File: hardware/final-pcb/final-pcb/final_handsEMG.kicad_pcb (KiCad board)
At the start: 2 copper layers, 47 parts, among them J1 Conn_02x13_Odd_Even, U1 ADS1299CPAG

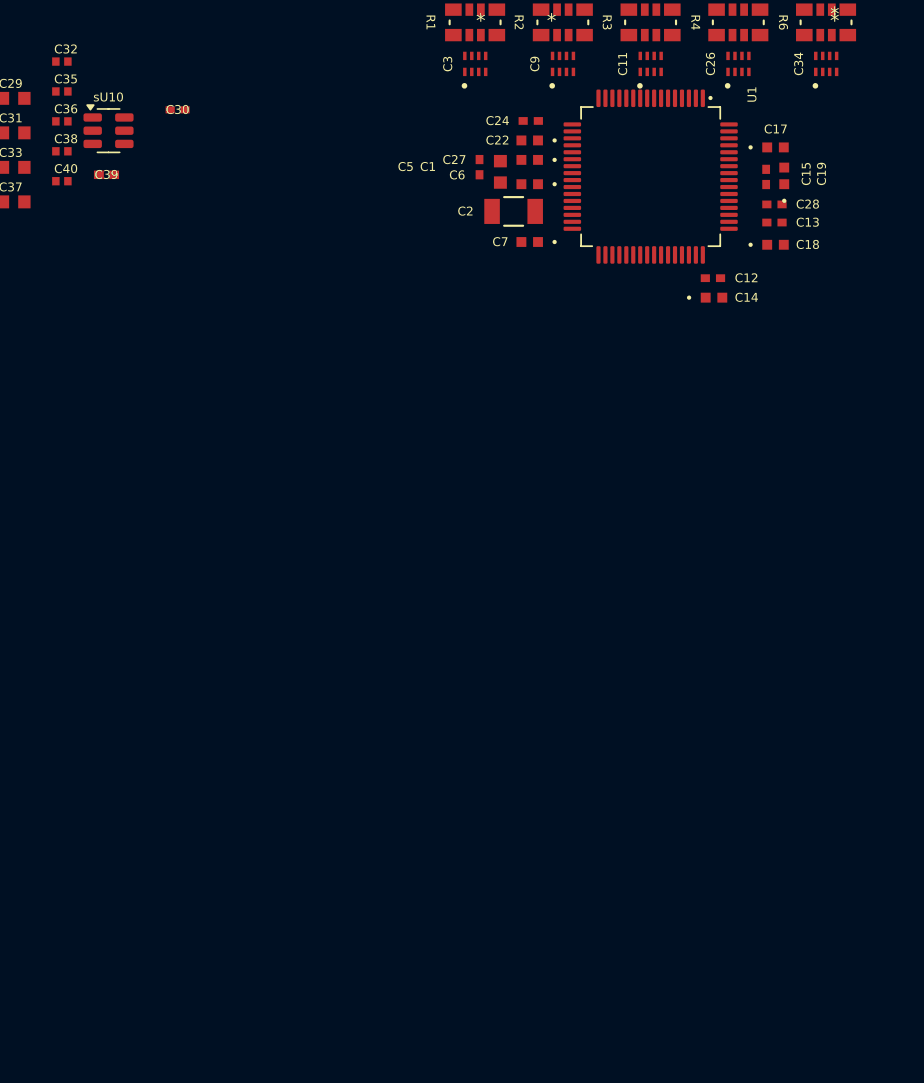
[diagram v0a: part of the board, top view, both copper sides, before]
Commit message: added stm32 decoupling circuitry and usb (3.24.25)
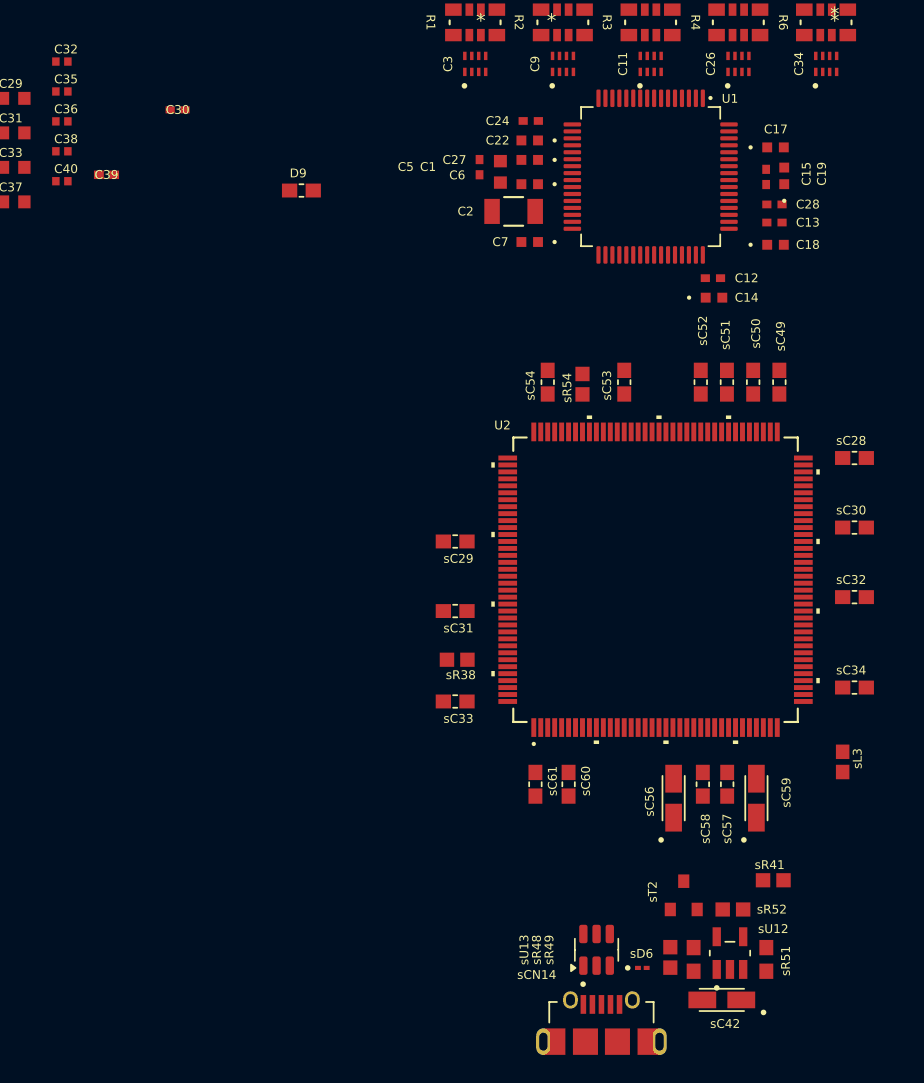
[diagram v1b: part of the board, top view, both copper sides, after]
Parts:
- added D9: D_Small, CC0603KRX7R7BB104:CAPC1608X90, F.Cu at (80.4, 62.0)
- added U2: STM32L496ZGT6, STM32L496ZGT6:LQFP144-20x20mm_STM, F.Cu at (105.8, 90.0)
- added sC28: 100nF, CC0603KRX7R7BB104:CAPC1608X90, F.Cu at (120.2, 81.2)
- added sC29: 100nF, CC0603KRX7R7BB104:CAPC1608X90, F.Cu at (91.5, 87.2)
- added sC30: 100nF, CC0603KRX7R7BB104:CAPC1608X90, F.Cu at (120.2, 86.2)
- added sC31: 100nF, CC0603KRX7R7BB104:CAPC1608X90, F.Cu at (91.5, 92.2)
- added sC32: 100nF, CC0603KRX7R7BB104:CAPC1608X90, F.Cu at (120.2, 91.2)
- added sC33: 100nF, CC0603KRX7R7BB104:CAPC1608X90, F.Cu at (91.5, 98.7)
- added sC34: 100nF, CC0603KRX7R7BB104:CAPC1608X90, F.Cu at (120.2, 97.7)
- added sC42: 4.7uF, TAJA475K016R:CAPMP3216X166, F.Cu at (110.6, 120.2)
- added sC49: 100nF, CC0603KRX7R7BB104:CAPC1608X90, F.Cu at (114.8, 75.8)
- added sC50: 100nF, CC0603KRX7R7BB104:CAPC1608X90, F.Cu at (112.9, 75.8)
- added sC51: 100nF, CC0603KRX7R7BB104:CAPC1608X90, F.Cu at (111.0, 75.8)
- added sC52: 4.7uF_X54_0603, CC0603KRX5R7BB475:CAPC1608X90, F.Cu at (109.1, 75.8)
- added sC53: 100nF, CC0603KRX7R7BB104:CAPC1608X90, F.Cu at (103.6, 75.8)
- added sC54: 4.7uF_X54_0603, CC0603KRX5R7BB475:CAPC1608X90, F.Cu at (98.1, 75.8)
- added sC56: 1uF, TAJA105K016R:CAPMP3216X166, F.Cu at (107.2, 105.7)
- added sC57: 100nF, CC0603KRX7R7BB104:CAPC1608X90, F.Cu at (111.0, 104.7)
- added sC58: 100nF, CC0603KRX7R7BB104:CAPC1608X90, F.Cu at (109.2, 104.7)
- added sC59: 1uF, TAJA105K016R:CAPMP3216X166, F.Cu at (113.1, 105.7)
- added sC60: 1uF_X5R_0603, CC0603KRX5R7BB105:CAPC1608X90, F.Cu at (99.6, 104.7)
- added sC61: 100nF, CC0603KRX7R7BB104:CAPC1608X90, F.Cu at (97.2, 104.7)
- added sCN14: USB_B_Micro, 47589-1001:MOLEX_47589-1001, F.Cu at (102.0, 123.5)
- added sD6: ESDALC6V1_1U2, ESDALC6V1-1U2:DIODE_ESDALC6V1-1U2, F.Cu at (104.9, 117.9)
- added sL3: FerriteBead_Small, FCM1608KF-601T05:FB0603, F.Cu at (119.3, 103.1)
- added sR38: 10K, RC0603FR-0710KL:RESC1607X60N, F.Cu at (91.6, 95.7)
- added sR41: 330, RC0603FR-07330RL:RESC1607X60N, F.Cu at (114.3, 111.6)
- added sR48: 22K, RC0603FR-0722KL:RESC1607X60N, F.Cu at (106.9, 117.1)
- added sR49: 47K, RC0603FR-0747KL:RESC1608X55, F.Cu at (108.6, 117.3)
- added sR51: 47K, RC0603FR-0747KL:RESC1608X55, F.Cu at (113.8, 117.3)
- added sR52: 10K, RC0603FR-0710KL:RESC1607X60N, F.Cu at (111.4, 113.7)
- added sR54: 10K, RC0603FR-0710KL:RESC1607X60N, F.Cu at (100.6, 75.9)
- added sT2: 9013, MMBT9013:SOT-23, F.Cu at (107.9, 112.7)
- added sU12: STMPS2151STR, STMPS2151STR:SOT95P280X145-5N, F.Cu at (111.2, 116.8)
- moved sU13 68.5 mm to (101.6, 116.6), turned to 90 degrees
- renumbered sU10 to sU13
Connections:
- sU13 pad 1: PA12 -> PA11
- sU13 pad 3: PA11 -> PA12
- sU13 pad 4: PA11 -> PA12
- sU13 pad 6: PA12 -> PA11

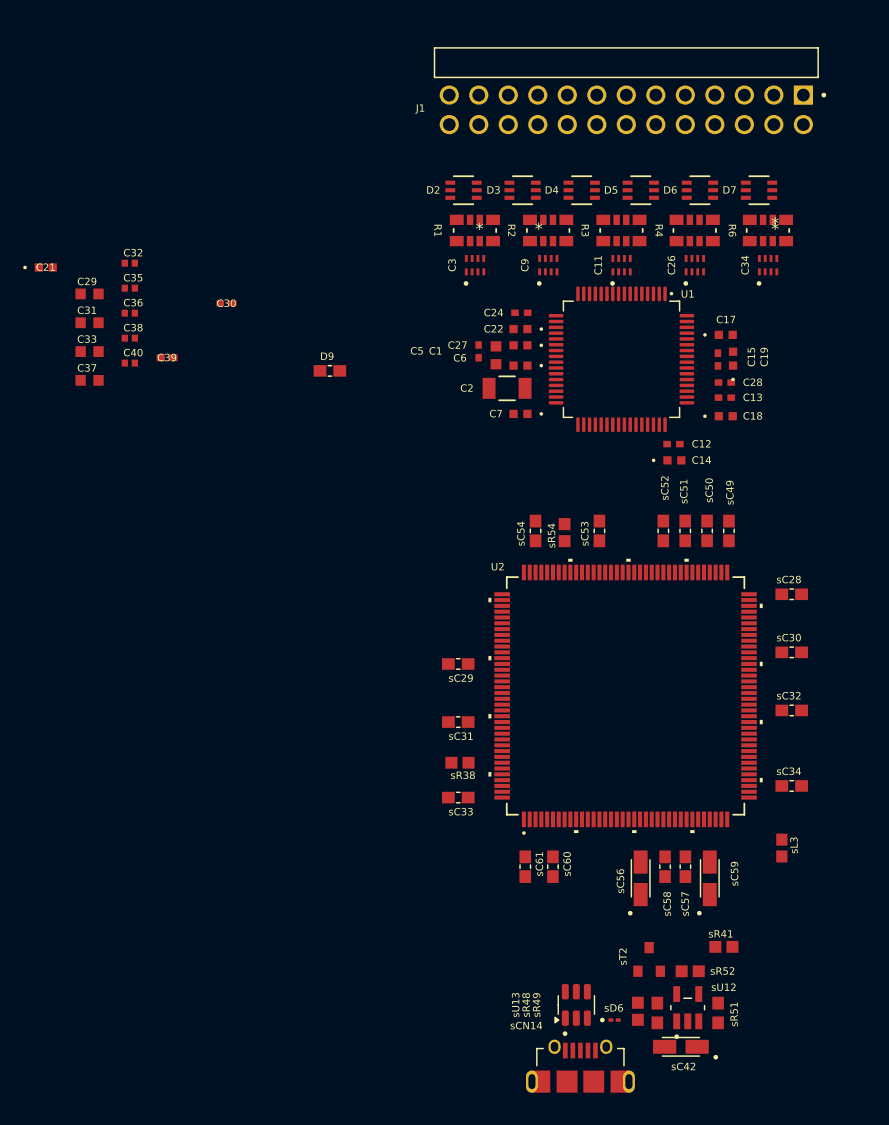
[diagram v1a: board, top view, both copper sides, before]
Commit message: basic routing (3.30.25)
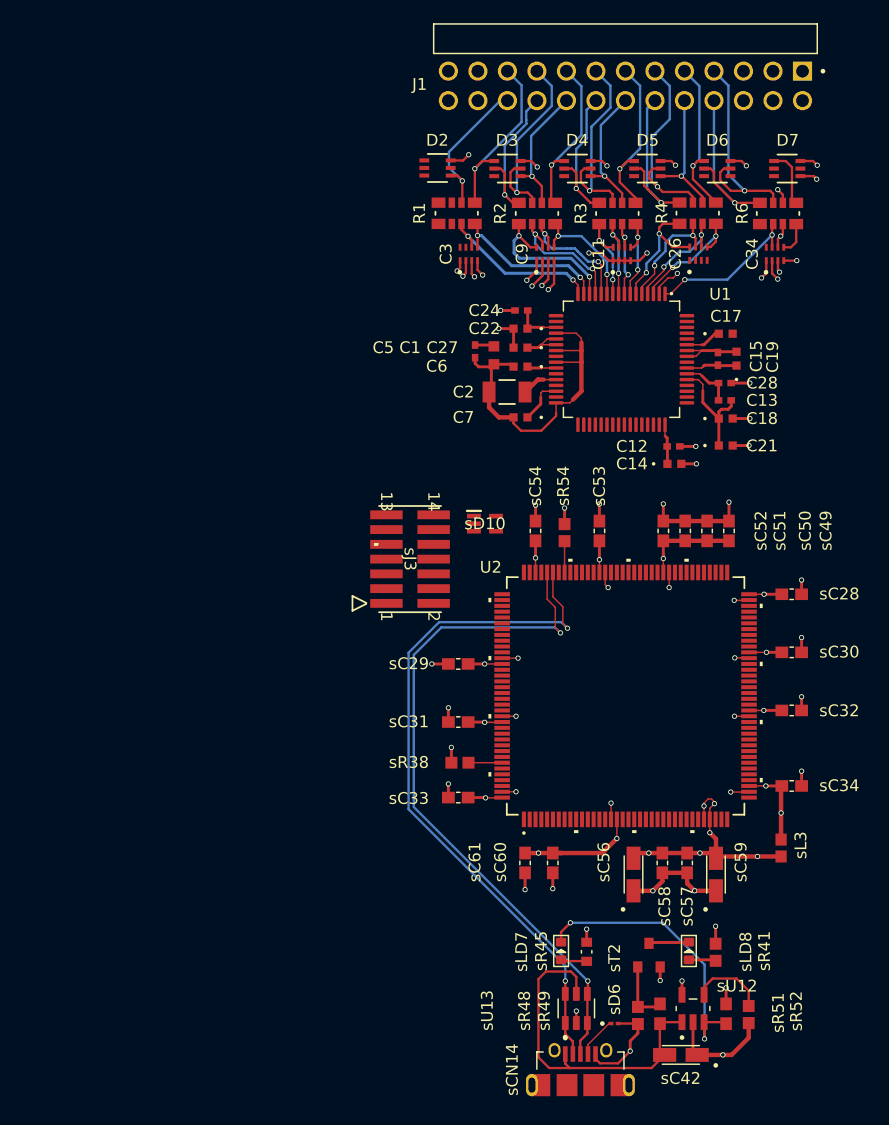
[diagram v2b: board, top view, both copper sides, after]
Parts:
- removed C29, C31, C33, C37: 10uF, GRM188C80G106KE47D:CAPC1608X90N
- removed C30: 0.01uF, CC0402KRX7R7BB103:CC0402N_YAG
- removed C32, C35, C36, C38, C40: 2.2uF, GRM155C80J225ME95D:CAPC1005X55N
- removed C39: 2.2uF, GRM155R61C225KE44D:CAP_GRM155R61C225KE44D_MUR
- removed D9: D_Small, CC0603KRX7R7BB104:CAPC1608X90
- added sD10: ESDALC6V1W5, ESDALC6V1W5:SOT65P210X110-5N, F.Cu at (93.8, 75.2)
- added sJ3: FTSH-107-01-L-DV-K, FTSH_107_01_L_DV_K:CON14_2X7_DUK_FTSH_SAI, F.Cu at (87.3, 78.2)
- added sLD7: Red, LED-SMD-RED-DIFFUSED_0603_:LED-0603, F.Cu at (100.3, 111.9)
- added sLD8: Green, SMD-LED-CLEAR-GREEN_0603_:LED-0603, F.Cu at (111.3, 111.9)
- added sR45: 620, RC0603FR-07620RL:RESC1608X55N, F.Cu at (102.5, 112.0)
- sU13: footprint Package_TO_SOT_SMD:SOT-23-6 -> USBLC6-2SC6:SOT95P280X145-6N
- moved C21 60.5 mm to (114.5, 68.4)
- moved sR52 6.26 mm to (116.5, 117.4), turned to -90 degrees
- moved D7 3.06 mm to (119.8, 44.6)
- moved D2 2.95 mm to (89.7, 44.5)
- moved D6 2.39 mm to (113.7, 44.6)
- moved D3 2.28 mm to (95.7, 44.6)
- moved R1 2.16 mm to (91.3, 48.4)
- moved J1 2.06 mm to (105.8, 33.4)
- moved D5 1.95 mm to (107.7, 44.6)
- moved D4 1.90 mm to (101.7, 44.6)
- moved R2 1.75 mm to (98.2, 48.5)
- moved R6 1.70 mm to (119.0, 48.5)
- moved R4 1.51 mm to (112.1, 48.4)
- moved R3 1.51 mm to (105.1, 48.5)
- moved C34 1.13 mm to (118.7, 51.9)
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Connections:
- net PA11 renamed USB_DN
- net PA12 renamed USB_DP
- U2 pad 25: /NRST -> NRST
- sC42 pad +: (no net) -> USB_VBUS
- sC42 pad -: (no net) -> GND
- sC56 pad -: (no net) -> GNDA
- sC59 pad +: (no net) -> AVDD
- sC59 pad -: (no net) -> GNDA
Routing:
- net GNDA: track 0.00 -> 61.7 mm, vias 0 -> 32
- net USB_DN: track 0.00 -> 60.7 mm, vias 0 -> 2
- net USB_DP: track 0.00 -> 60.3 mm, vias 0 -> 2
- net DVDD: track 0.00 -> 58.4 mm, vias 0 -> 17
- net GND: track 0.00 -> 57.7 mm, vias 0 -> 28
- net AVSS: track 0.00 -> 46.1 mm
- net AVDD: track 0.00 -> 36.8 mm, vias 0 -> 6
- net USB_VBUS: track 0.00 -> 31.2 mm, vias 0 -> 1
- net Net-(sLD7-K): track 0.00 -> 24.8 mm, vias 0 -> 2
- net 8N: track 0.00 -> 18.9 mm, vias 0 -> 1
- net 6N: track 0.00 -> 17.9 mm, vias 0 -> 1
- net 4N: track 0.00 -> 17.3 mm, vias 0 -> 1
- net 2N: track 0.00 -> 17.2 mm, vias 0 -> 1
- net 8P: track 0.00 -> 16.1 mm, vias 0 -> 1
- net 1N: track 0.00 -> 15.5 mm, vias 0 -> 1
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
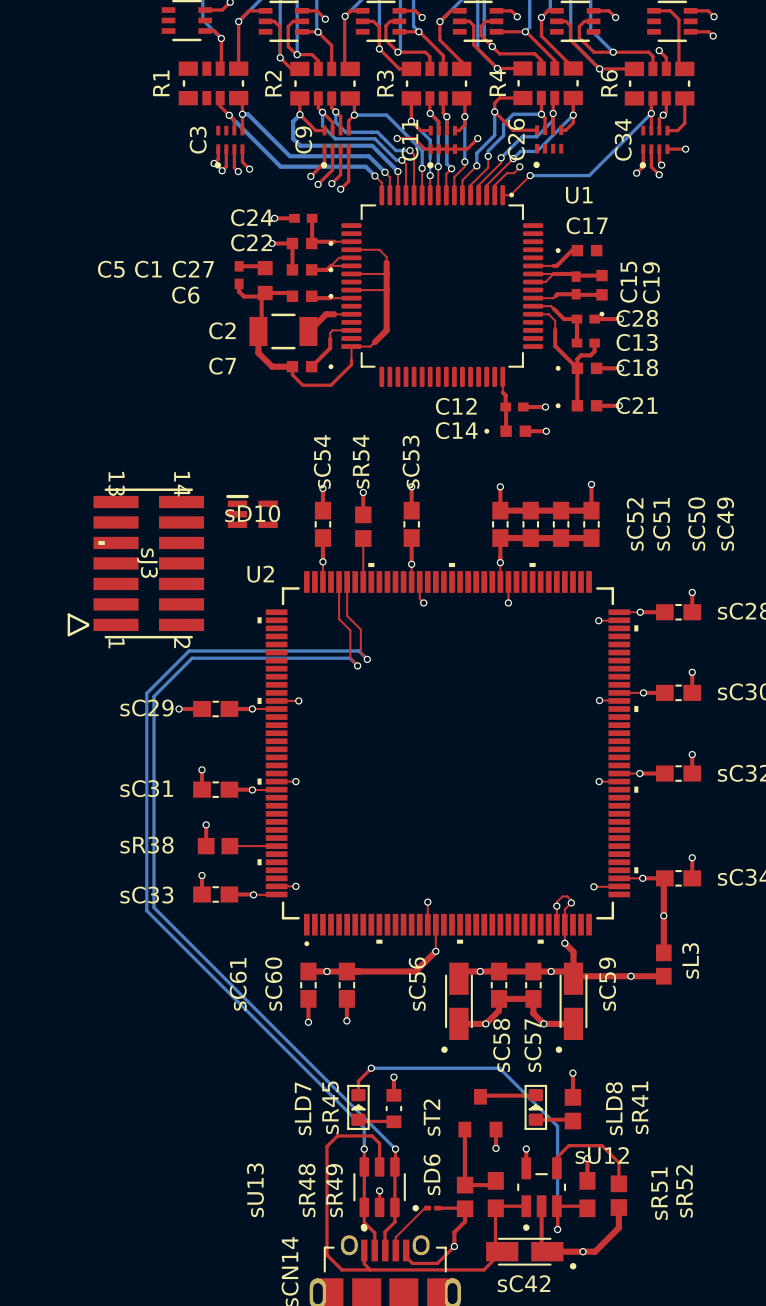
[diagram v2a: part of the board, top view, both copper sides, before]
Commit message: added ltc3586 and ads1299 LDOs (3.31.25)
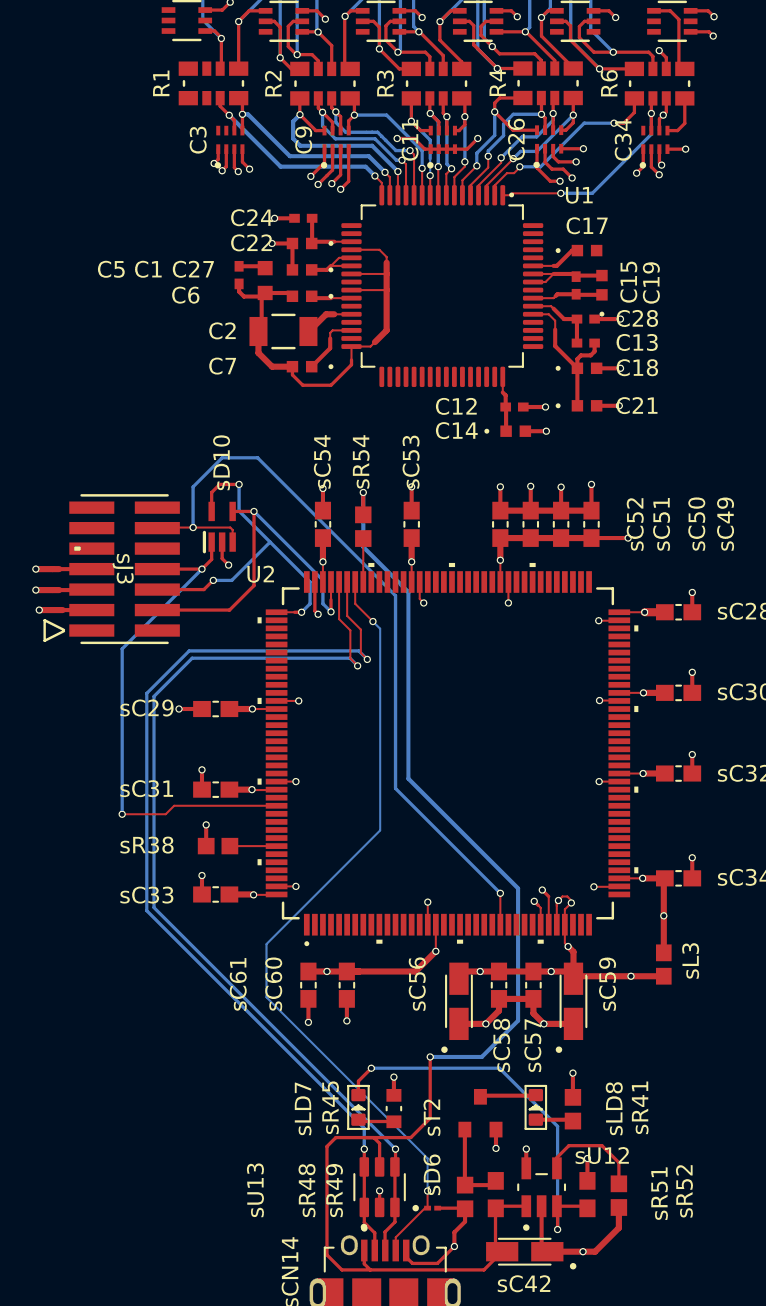
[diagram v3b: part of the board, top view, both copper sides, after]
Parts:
- moved sD10 2.05 mm to (91.8, 75.9), turned to 90 degrees
- moved sJ3 1.54 mm to (85.8, 78.5)
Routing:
- net USB_VBUS: track 31.2 -> 82.7 mm, vias 1 -> 2
- net NRST: track 0.00 -> 48.1 mm, vias 0 -> 2
- net PA10: track 3.54 -> 50.1 mm, vias 0 -> 2
- net PB3: track 0.00 -> 31.7 mm, vias 0 -> 2
- net PA14: track 0.00 -> 23.3 mm, vias 0 -> 3
- net PA13: track 0.00 -> 22.6 mm, vias 0 -> 2
- net GND: track 57.7 -> 71.3 mm, vias 28 -> 34
- net GNDA: track 61.7 -> 74.9 mm, vias 32 -> 38
- net IN8P: track 2.66 -> 12.0 mm, vias 1 -> 2
- net DVDD: track 58.4 -> 63.9 mm, vias 17 -> 19
- net IN8N: track 13.3 -> 14.1 mm
